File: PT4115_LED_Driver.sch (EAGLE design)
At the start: 59 parts, among them IC1 PCA9685PW, IC2 TMP421

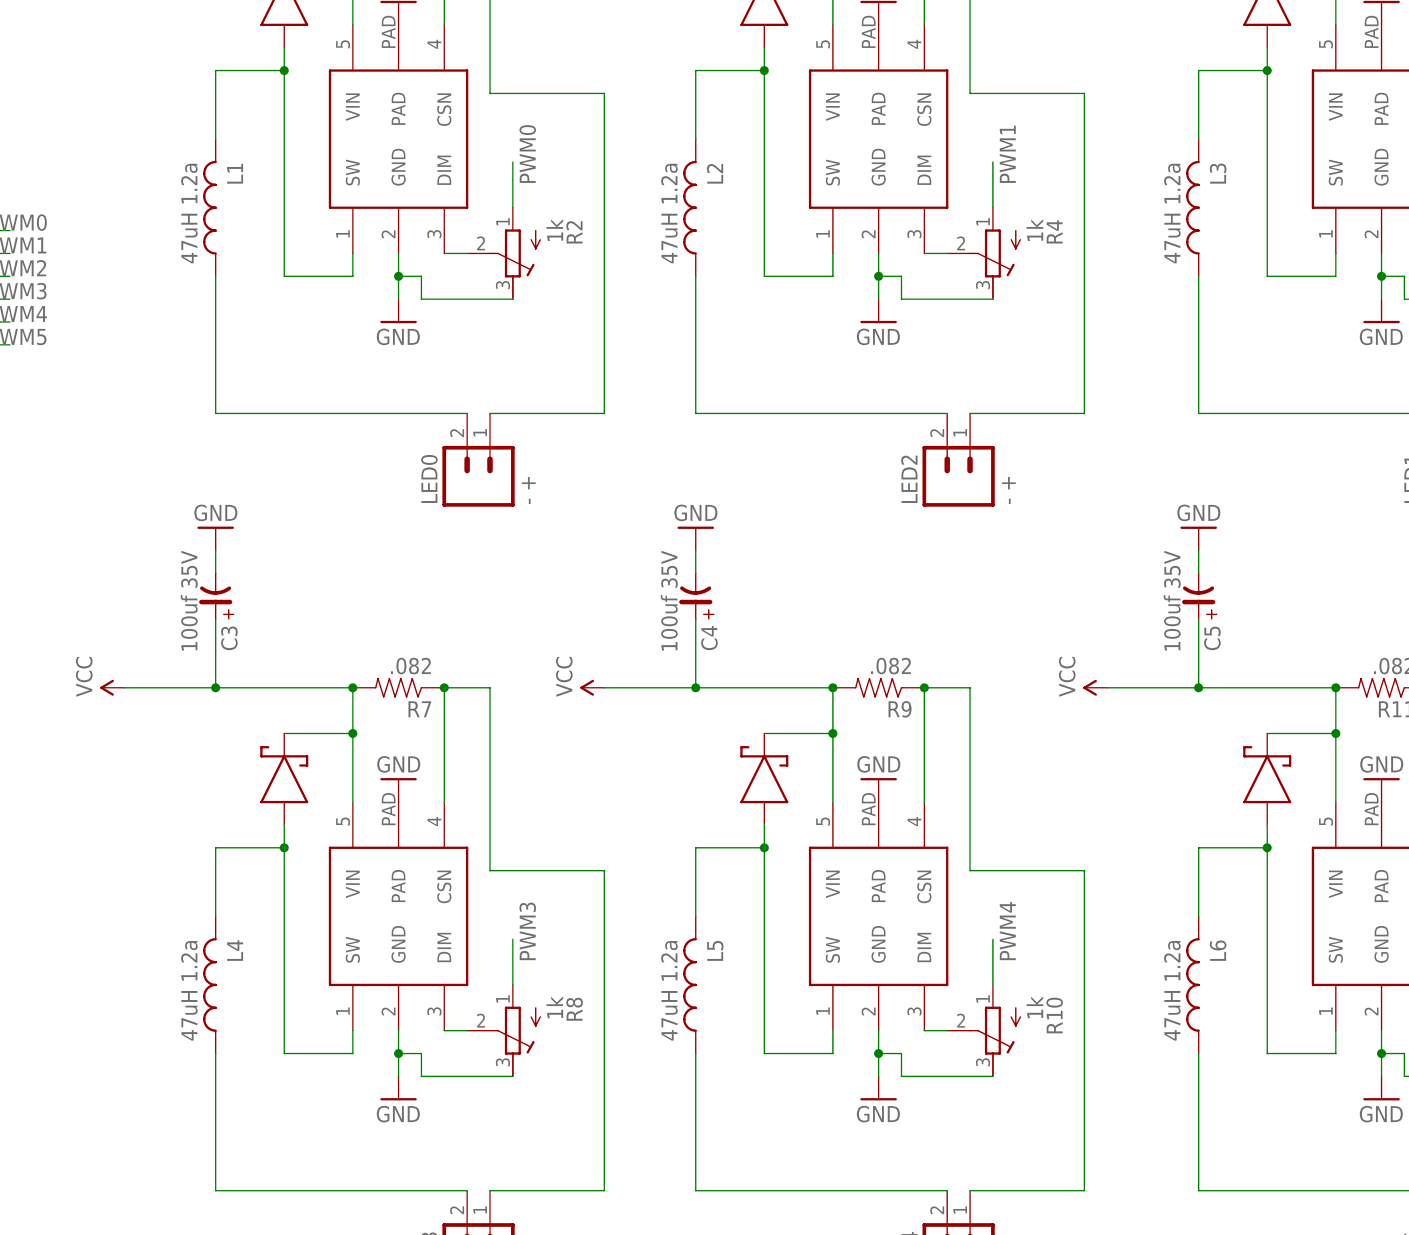
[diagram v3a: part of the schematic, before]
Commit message: Switched to larger pad for inductor to source 1.2a part.  Switched top plane from 5V to GND.
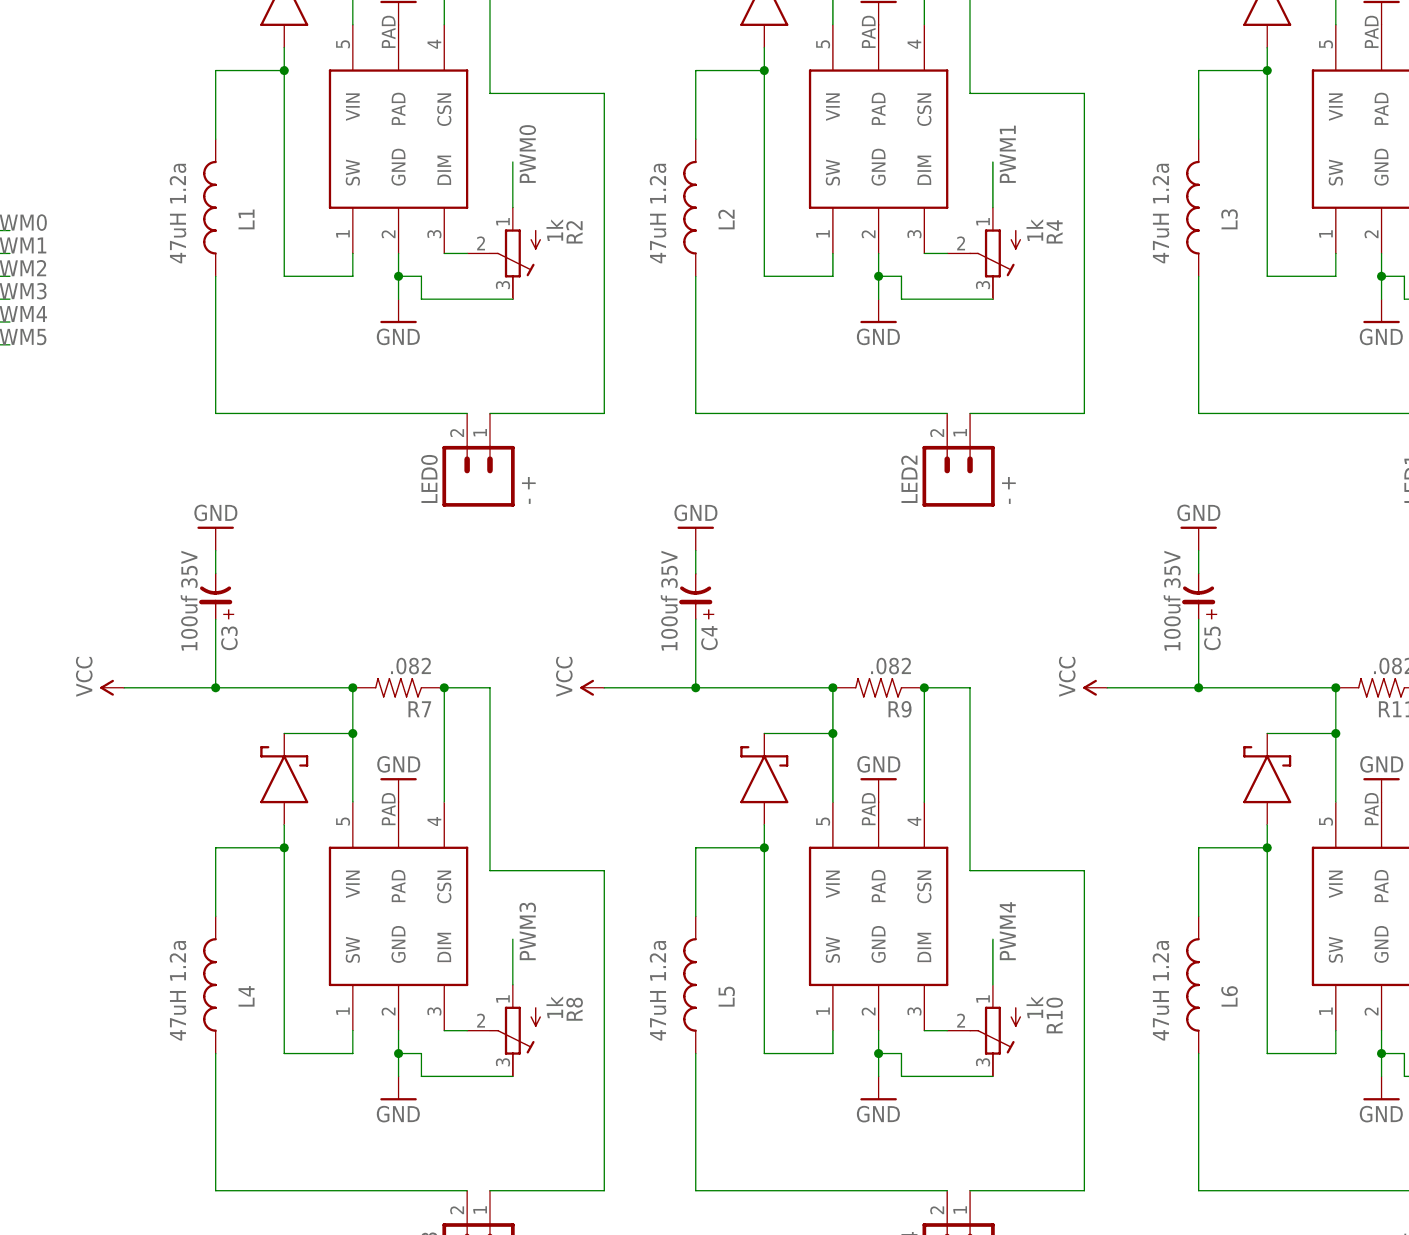
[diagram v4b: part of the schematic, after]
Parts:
- L1, L2, L3, L4, L5, L6: device rcl:L-USL4532P -> SparkFun:INDUCTORCR54

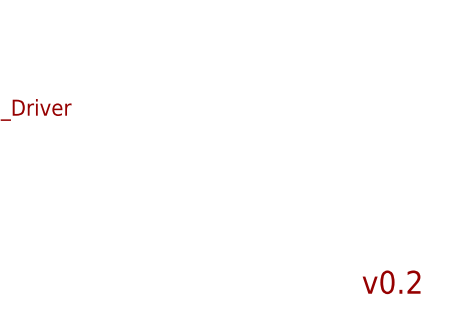
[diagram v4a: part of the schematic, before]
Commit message: Fixed issues with ground pad on TMP421 address jumper.  Moved mounting holes to provide better clearance.  Fixed silkscreen labeling problems with PCA9685 jumper and TMP421 external temp jumper.
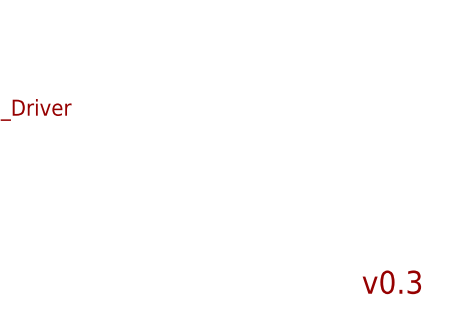
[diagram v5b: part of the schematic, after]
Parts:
- ON: device led:LEDCHIPLED_0603 -> led:LEDCHIPLED_0805
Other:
- note added: "v0.3"
- note removed: "v0.2"
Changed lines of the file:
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@@
 <part name="GND32" library="supply1" deviceset="GND" device=""/>
 <part name="R13" library="SparkFun" deviceset="RESISTOR" device="0603-RES" value="1k"/>
-<part name="ON" library="led" deviceset="LED" device="CHIPLED_0603" value="GREEN"/>
+<part name="ON" library="led" deviceset="LED" device="CHIPLED_0805" value="GREEN"/>
 <part name="GND33" library="supply1" deviceset="GND" device=""/>
 </parts>
@@
 <sheet>
 <plain>
-<text x="245.11" y="-88.9" size="2.54" layer="94" font="vector">v0.2</text>
+<text x="245.11" y="-88.9" size="2.54" layer="94" font="vector">v0.3</text>
 <text x="160.02" y="-89.44" size="1.778" layer="94" font="vector">I2C controlled LED driver</text>
 <text x="160.02" y="-69.12" size="1.778" layer="94" font="vector">https://github.com/brunnels/PT4115_LED_Driver</text>
